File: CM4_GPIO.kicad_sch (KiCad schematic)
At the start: 21 parts, among them J1 Conn_02x07_Odd_Even, J2 Conn_01x03, J3 Conn_01x03, J4 THD-20-R, J8 Micro_SD_Card_Det, U2 74LVC1G07SE-7, U3 74LVC1G07SE-7, U6 RT9742GGJ5

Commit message: worked some more on converting components (unfinished)
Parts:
- removed J8: Micro_SD_Card_Det, CM4IO:SDCARD_MOLEX_503398-1892, symbol Connector:Micro_SD_Card_Det
- removed U6: RT9742GGJ5, Package_TO_SOT_SMD:SOT-23-5, symbol CM4IO:RT9742GGJ5
- added C50: 100n, Capacitor_SMD:C_0402_1005Metric, symbol Device:C
- added J10: Micro_SD_Card_Det, CM4IO:SDCARD_MOLEX_503398-1892, symbol Connector:Micro_SD_Card_Det
- added J8: THD-02-R, Connector_PinHeader_2.54mm:PinHeader_2x02_P2.54mm_Vertical, symbol Connector_Generic:Conn_02x02_Odd_Even
- added R36: 470R, Resistor_SMD:R_0402_1005Metric, symbol Device:R
- added R37: 12K 1%, Resistor_SMD:R_0402_1005Metric, symbol Device:R
- added U17, U6: TPD4EUSB30, Package_SON:USON-10_2.5x1.0mm_P0.5mm, symbol CM4IO:TPD4EUSB30
- added U18: RT9742GGJ5, Package_TO_SOT_SMD:SOT-23-5, symbol CM4IO:RT9742GGJ5
- added U19: MagJack-A70-112-331N126, CM4IO:TRJG0926HENL, symbol CM4IO:MagJack-A70-112-331N126
- R9: value 12K 1% -> 470R; Field5 9239367 -> 9239197; Field6 MCR01MZPF1202 -> RK73G1ETQTP4700D; Field7 Rohm -> KOA EUROPE GMBH; Field8 (none) -> 120887981; Part Description Resistor 12K M1005 1% 63mW -> Resistor 470R M1005 1% 63mW
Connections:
- net +3.3v: now also R37.1, U18.5 (IN), U19.15 (LEDG_A), U19.17 (LEDY_A); no longer R9.1
- net +5v: no longer Module1.77 (+5v_(Input)), Module1.79 (+5v_(Input)), Module1.81 (+5v_(Input)), Module1.83 (+5v_(Input)), Module1.85 (+5v_(Input)), Module1.87 (+5v_(Input))
- net ETH_LEDG: now also R9.2
- net ETH_LEDY: now also R36.2
- net GND: now also C50.2, J10.11 (SHIELD), J10.6 (VSS), U17.3 (GND), U17.8 (GND), U18.2 (GND), U19.19 (SHIELD), U19.20 (SHIELD), U6.3 (GND), U6.8 (GND)
- net SD_CLK: now also J10.5 (CLK)
- net SD_CMD: now also J10.3 (CMD)
- net SD_DAT0: now also J10.7 (DAT0)
- net SD_DAT1: now also J10.8 (DAT1)
- net SD_DAT2: now also J10.1 (DAT2)
- net SD_DAT3: now also J10.2 (DAT3/CD)
- net SD_PWR: now also J10.4 (VDD), U18.1 (OUT)
- net SD_PWR_ON: now also R37.2, U18.4 (EN); no longer R9.2
- net TRD0_N: now also U17.4 (D2+), U17.7, U19.2 (TRD0-); no longer Module1.10 (Ethernet_Pair0_N)
- net TRD0_P: now also U17.5 (D2-), U17.6, U19.1 (TRD0+); no longer Module1.12 (Ethernet_Pair0_P)
- net TRD1_N: now also U17.2 (D1-), U17.9, U19.6 (TRD1-); no longer Module1.6 (Ethernet_Pair1_N)
- net TRD1_P: now also U17.1 (D1+), U17.10, U19.3 (TRD1+); no longer Module1.4 (Ethernet_Pair1_P)
- net TRD2_N: now also U19.8 (TRD2-), U6.4 (D2+), U6.7
- net TRD2_P: now also U19.7 (TRD2+), U6.5 (D2-), U6.6
- net TRD3_N: now also U19.10 (TRD3-), U6.2 (D1-), U6.9
- net TRD3_P: now also U19.9 (TRD3+), U6.1 (D1+), U6.10
- net at R5.2: now also J10.10 (DET_A)
- net at R6.2: now also J10.9 (DET_B)
- net CAM_GPIO: no longer names the net of Module1.97 (Camera_GPIO)
- new net: R9.1, U19.16 (LEDG_K)
- new net: R36.1, U19.18 (LEDY_K)
- new net: C50.1, U19.4 (CT), U19.5 (CT)
- new net +5V: Module1.77 (+5v_(Input)), Module1.79 (+5v_(Input)), Module1.81 (+5v_(Input)), Module1.83 (+5v_(Input)), Module1.85 (+5v_(Input)), Module1.87 (+5v_(Input))
- new net TR0_TAP: J8.3 (Pin_3), U19.11 (VC1)
- new net TR1_TAP: J8.1 (Pin_1), U19.12 (VC2)
- new net TR2_TAP: J8.2 (Pin_2), U19.13 (VC3)
- new net TR3_TAP: J8.4 (Pin_4), U19.14 (VC4)
- no-connect marks 7 -> 12
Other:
- note added: "Ethernet"
- note added: "Ethernet POE Protection"
- note added: "POE Header"

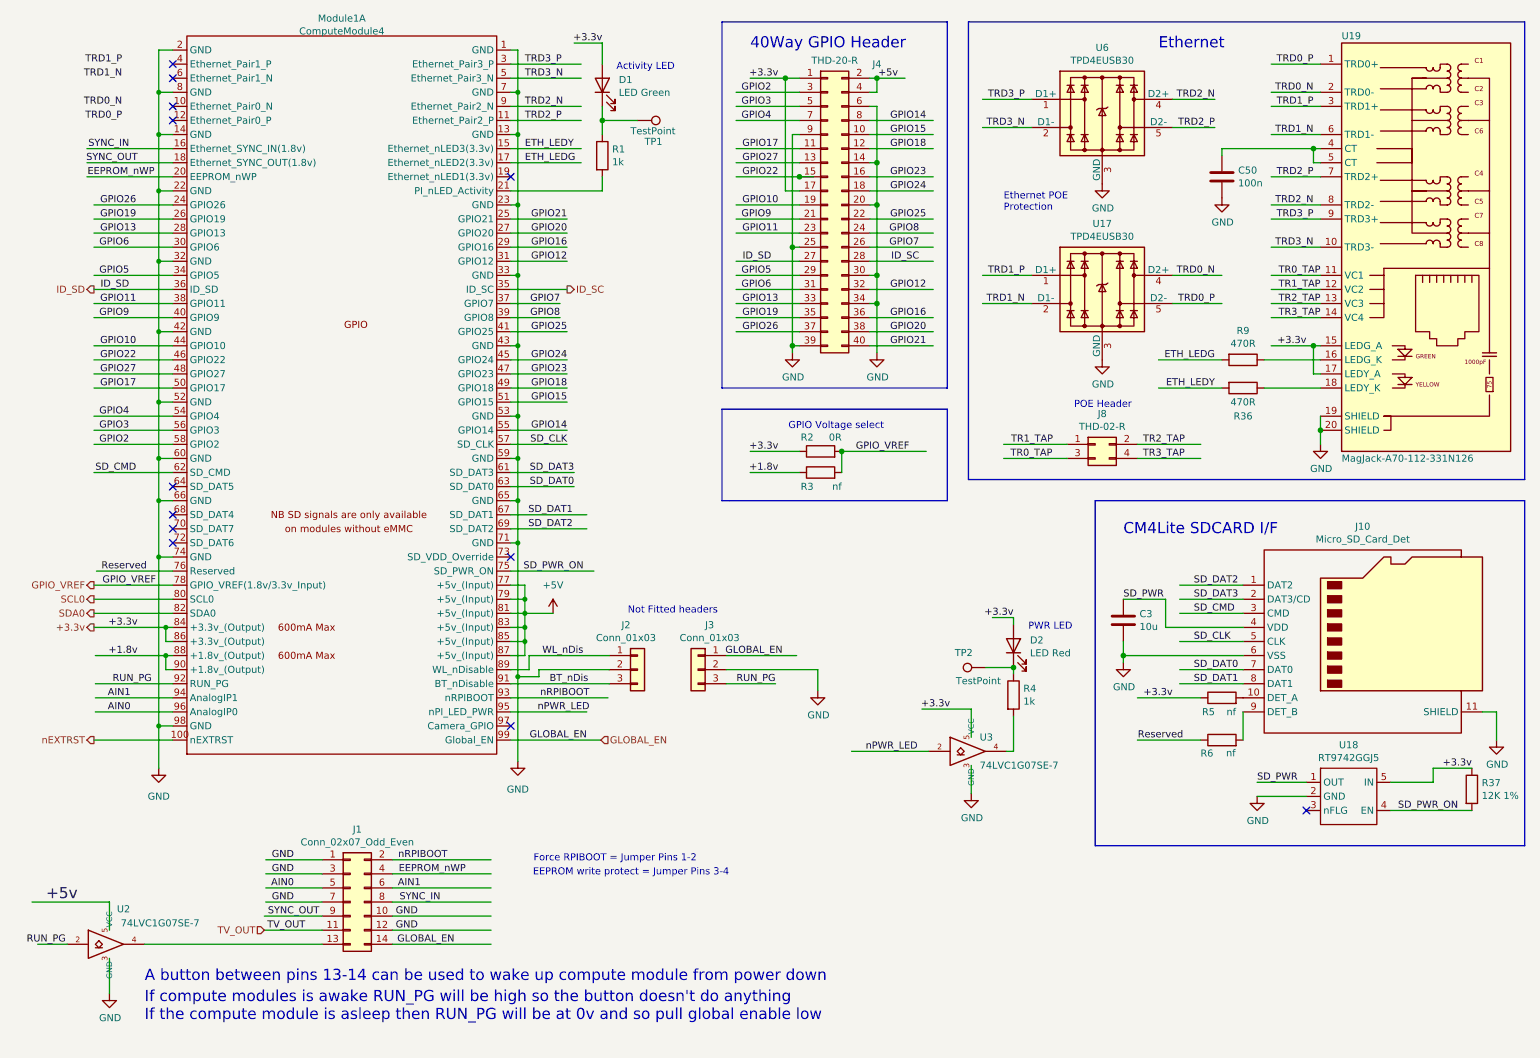
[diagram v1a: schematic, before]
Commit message: power dist, hdmi, and rtc are done; finding a new usb hub
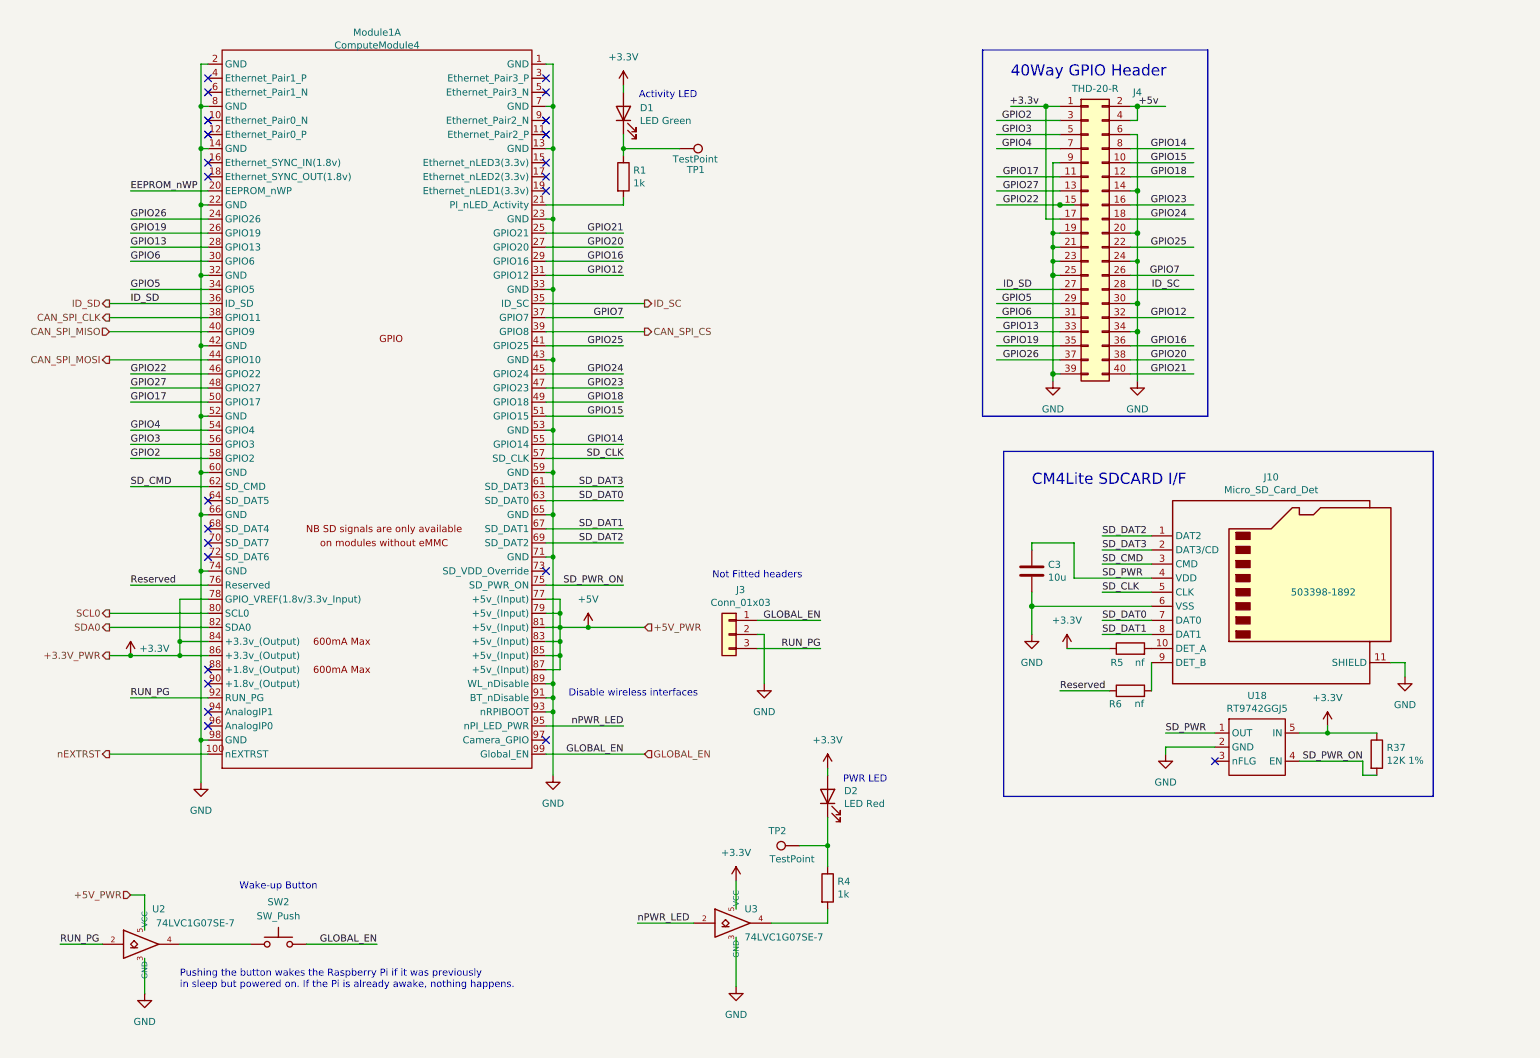
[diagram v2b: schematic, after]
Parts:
- removed C50: 100n, Capacitor_SMD:C_0402_1005Metric, symbol Device:C
- removed J1: Conn_02x07_Odd_Even, Connector_PinHeader_2.54mm:PinHeader_2x07_P2.54mm_Vertical, symbol Connector_Generic:Conn_02x07_Odd_Even
- removed J2: Conn_01x03, Connector_PinHeader_2.54mm:PinHeader_1x03_P2.54mm_Vertical, symbol Connector_Generic:Conn_01x03
- removed J8: THD-02-R, Connector_PinHeader_2.54mm:PinHeader_2x02_P2.54mm_Vertical, symbol Connector_Generic:Conn_02x02_Odd_Even
- removed R2: 0R, Resistor_SMD:R_0805_2012Metric_Pad1.15x1.40mm_HandSolder, symbol Device:R
- removed R3: nf, Resistor_SMD:R_0805_2012Metric_Pad1.15x1.40mm_HandSolder, symbol Device:R
- removed R36, R9: 470R, Resistor_SMD:R_0402_1005Metric, symbol Device:R
- removed U17, U6: TPD4EUSB30, Package_SON:USON-10_2.5x1.0mm_P0.5mm, symbol CM4IO:TPD4EUSB30
- removed U19: MagJack-A70-112-331N126, CM4IO:TRJG0926HENL, symbol CM4IO:MagJack-A70-112-331N126
- added SW2: SW_Push, symbol Switch:SW_Push
- D2: Field5 LTST-S270KRKT -> LTST-S270KRKT
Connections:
- net BT_nDis is gone; now on net GND: Module1.91 (BT_nDisable)
- net WL_nDis is gone; now on net GND: Module1.89 (WL_nDisable)
- net nRPIBOOT is gone; now on net GND: Module1.93 (nRPIBOOT)
- net +3.3v: no longer D1.2 (A), D2.2 (A), Module1.84 (+3.3v_(Output)), Module1.86 (+3.3v_(Output)), R37.1, R5.1, U18.5 (IN), U3.5 (VCC)
- net +5V: now also U2.5 (VCC)
- net +5v: no longer U2.5 (VCC)
- net GLOBAL_EN: now also SW2.2
- net GND: now also J4.19 (Pin_19), J4.21 (Pin_21), J4.23 (Pin_23), J4.24 (Pin_24)
- net at U2.4: now also SW2.1
- net +1.8v: no longer names the net of Module1.88 (+1.8v_(Output))
- net +1.8v: no longer Module1.90 (+1.8v_(Output))
- net AIN0: no longer names the net of Module1.96 (AnalogIP0)
- net AIN1: no longer names the net of Module1.94 (AnalogIP1)
- net ETH_LEDG: no longer names the net of Module1.17 (Ethernet_nLED2(3.3v))
- net ETH_LEDY: no longer names the net of Module1.15 (Ethernet_nLED3(3.3v))
- net GPIO10 renamed CAN_SPI_MOSI
- net CAN_SPI_MOSI: no longer J4.19 (Pin_19)
- net GPIO11 renamed CAN_SPI_CLK
- net CAN_SPI_CLK: no longer J4.23 (Pin_23)
- net GPIO8 renamed CAN_SPI_CS
- net CAN_SPI_CS: no longer J4.24 (Pin_24)
- net GPIO9 renamed CAN_SPI_MISO
- net CAN_SPI_MISO: no longer J4.21 (Pin_21)
- net GPIO_VREF renamed +3.3V
- net +3.3V: now also D1.2 (A), D2.2 (A), Module1.84 (+3.3v_(Output)), Module1.86 (+3.3v_(Output)), R37.1, R5.1, U18.5 (IN), U3.5 (VCC)
- net SYNC_IN: no longer names the net of Module1.16 (Ethernet_SYNC_IN(1.8v))
- net SYNC_OUT: no longer names the net of Module1.18 (Ethernet_SYNC_OUT(1.8v))
- net TRD2_N: no longer names the net of Module1.9 (Ethernet_Pair2_N)
- net TRD2_P: no longer names the net of Module1.11 (Ethernet_Pair2_P)
- net TRD3_N: no longer names the net of Module1.5 (Ethernet_Pair3_N)
- net TRD3_P: no longer names the net of Module1.3 (Ethernet_Pair3_P)
- no-connect marks 12 -> 24
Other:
- note added: "Disable wireless interfaces"
- note added: "Pushing the button wakes the Raspberry Pi if it was previously in sleep but powered on. If the Pi is already awake, nothing happens."
- note added: "Wake-up Button"
- note removed: "A button between pins 13-14 can be used to wake up compute module from power down"
- note removed: "EEPROM write protect = Jumper Pins 3-4"
- note removed: "Ethernet"
- note removed: "Ethernet POE Protection"
- note removed: "Force RPIBOOT = Jumper Pins 1-2"
- note removed: "GPIO Voltage select"
- note removed: "If compute modules is awake RUN_PG will be high so the button doesn't do anything If the compute module is asleep then RUN_PG will be at 0v and so pull global enable low"
- note removed: "POE Header"
- moved on the sheet: C3, D1, J10, J3, J4, Module1A, R1, R37, R4, R5, R6, TP1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

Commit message: made more changes
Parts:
- removed Module1: ComputeModule4, CM4IO:Raspberry-Pi-4-Compute-Module, symbol CM4IO:ComputeModule4-CM4
- added Module2: ComputeModule4-CM4, CM4IO:Raspberry-Pi-4-Compute-Module, symbol CM4IO:ComputeModule4-CM4
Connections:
- net CAN_SPI_CLK: now also Module2.38 (GPIO11)
- net CAN_SPI_CS: now also Module2.39 (GPIO8)
- net CAN_SPI_MISO: now also Module2.40 (GPIO9)
- net CAN_SPI_MOSI: now also Module2.44 (GPIO10)
- net EEPROM_nWP: now also Module2.20 (EEPROM_nWP)
- net GLOBAL_EN: now also Module2.99 (Global_EN)
- net GND: now also Module2.1 (GND), Module2.13 (GND), Module2.14 (GND), Module2.2 (GND), Module2.22 (GND), Module2.23 (GND), Module2.32 (GND), Module2.33 (GND), Module2.42 (GND), Module2.43 (GND), Module2.52 (GND), Module2.53 (GND), Module2.59 (GND), Module2.60 (GND), Module2.65 (GND), Module2.66 (GND), Module2.7 (GND), Module2.71 (GND), Module2.74 (GND), Module2.8 (GND), Module2.89 (WiFi_nDisable), Module2.91 (BT_nDisable), Module2.93 (nRPIBOOT), Module2.98 (GND)
- net GPIO12: now also Module2.31 (GPIO12)
- net GPIO13: now also Module2.28 (GPIO13)
- net GPIO14: now also Module2.55 (GPIO14)
- net GPIO15: now also Module2.51 (GPIO15)
- net GPIO16: now also Module2.29 (GPIO16)
- net GPIO17: now also Module2.50 (GPIO17)
- net GPIO18: now also Module2.49 (GPIO18)
- net GPIO19: now also Module2.26 (GPIO19)
- net GPIO2: now also Module2.58 (GPIO2)
- net GPIO20: now also Module2.27 (GPIO20)
- net GPIO21: now also Module2.25 (GPIO21)
- net GPIO22: now also Module2.46 (GPIO22)
- net GPIO23: now also Module2.47 (GPIO23)
- net GPIO24: now also Module2.45 (GPIO24)
- net GPIO25: now also Module2.41 (GPIO25)
- net GPIO26: now also Module2.24 (GPIO26)
- net GPIO27: now also Module2.48 (GPIO27)
- net GPIO3: now also Module2.56 (GPIO3)
- net GPIO4: now also Module2.54 (GPIO4)
- net GPIO5: now also Module2.34 (GPIO5)
- net GPIO6: now also Module2.30 (GPIO6)
- net GPIO7: now also Module2.37 (GPIO7)
- net ID_SC: now also Module2.35 (ID_SC)
- net ID_SD: now also Module2.36 (ID_SD)
- net RUN_PG: now also Module2.92 (RUN_PG)
- net Reserved: now also Module2.76 (Reserved)
- net SCL0: now also Module2.80 (SCL0)
- net SDA0: now also Module2.82 (SDA0)
- net SD_CLK: now also Module2.57 (SD_CLK)
- net SD_CMD: now also Module2.62 (SD_CMD)
- net SD_DAT0: now also Module2.63 (SD_DAT0)
- net SD_DAT1: now also Module2.67 (SD_DAT1)
- net SD_DAT2: now also Module2.69 (SD_DAT2)
- net SD_DAT3: now also Module2.61 (SD_DAT3)
- net SD_PWR_ON: now also Module2.75 (SD_PWR_ON)
- net nEXTRST: now also Module2.100 (nEXTRST)
- net nPWR_LED: now also Module2.95 (nPI_LED_PWR)
- net at R1.2: now also Module2.21 (PI_nLED_Activity)
- net +5V renamed +5V_PWR
- net +5V_PWR: now also Module2.77 (+5v_(Input)), Module2.79 (+5v_(Input)), Module2.81 (+5v_(Input)), Module2.83 (+5v_(Input)), Module2.85 (+5v_(Input)), Module2.87 (+5v_(Input))
- new net +3.3V_PWR: Module2.78 (GPIO_VREF(1.8v/3.3v_Input)), Module2.84 (+3.3v_(Output)), Module2.86 (+3.3v_(Output))

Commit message: finished USB i think, working on general gpio in more detail
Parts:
- removed J10: Micro_SD_Card_Det, CM4IO:SDCARD_MOLEX_503398-1892, symbol Connector:Micro_SD_Card_Det
- removed R37: 12K 1%, Resistor_SMD:R_0402_1005Metric, symbol Device:R
- removed R5, R6: nf, Resistor_SMD:R_0402_1005Metric, symbol Device:R
- removed U18: RT9742GGJ5, Package_TO_SOT_SMD:SOT-23-5, symbol CM4IO:RT9742GGJ5
- added C10, C11, C6, C7, C8, C9: 100n, Capacitor_SMD:C_0402_1005Metric, symbol Device:C
- added C5: 10u, Capacitor_SMD:C_0805_2012Metric, symbol Device:C
- added U8: 74AUC1G07, symbol 74xGxx:74AUC1G07
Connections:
- net +3.3V is gone; now on net +3.3V_PWR: D1.2 (A), D2.2 (A), U3.5 (VCC)
- net SD_PWR is gone; now on net +3.3V_PWR: C3.1
- net +3.3V_PWR: now also C10.1, C11.1, C5.1, C6.1, C7.1, C8.1, C9.1
- net GND: now also C10.2, C11.2, C5.2, C6.2, C7.2, C8.2, C9.2
- net Reserved: no longer names the net of Module2.76 (Reserved)
- net SD_CLK: no longer names the net of Module2.57 (SD_CLK)
- net SD_CMD: no longer names the net of Module2.62 (SD_CMD)
- net SD_DAT0: no longer names the net of Module2.63 (SD_DAT0)
- net SD_DAT1: no longer names the net of Module2.67 (SD_DAT1)
- net SD_DAT2: no longer names the net of Module2.69 (SD_DAT2)
- net SD_DAT3: no longer names the net of Module2.61 (SD_DAT3)
- net SD_PWR_ON: no longer names the net of Module2.75 (SD_PWR_ON)
- no-connect marks 24 -> 30
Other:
- note added: "Power LED must be buffered"
- note removed: "CM4Lite SDCARD I/F"
